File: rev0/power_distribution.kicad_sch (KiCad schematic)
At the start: 81 parts, among them Q1 PMOS, Q10 2PNP, Q11 2NPN, Q12 PMOS, Q13 2PNP, Q14 2PNP, Q15 2PNP, Q2 PMOS, Q3 2NPN, Q4 PMOS, Q5 PMOS, Q6 PMOS, Q7 PMOS, Q8 2NPN, Q9 PMOS, U1 PAC1954

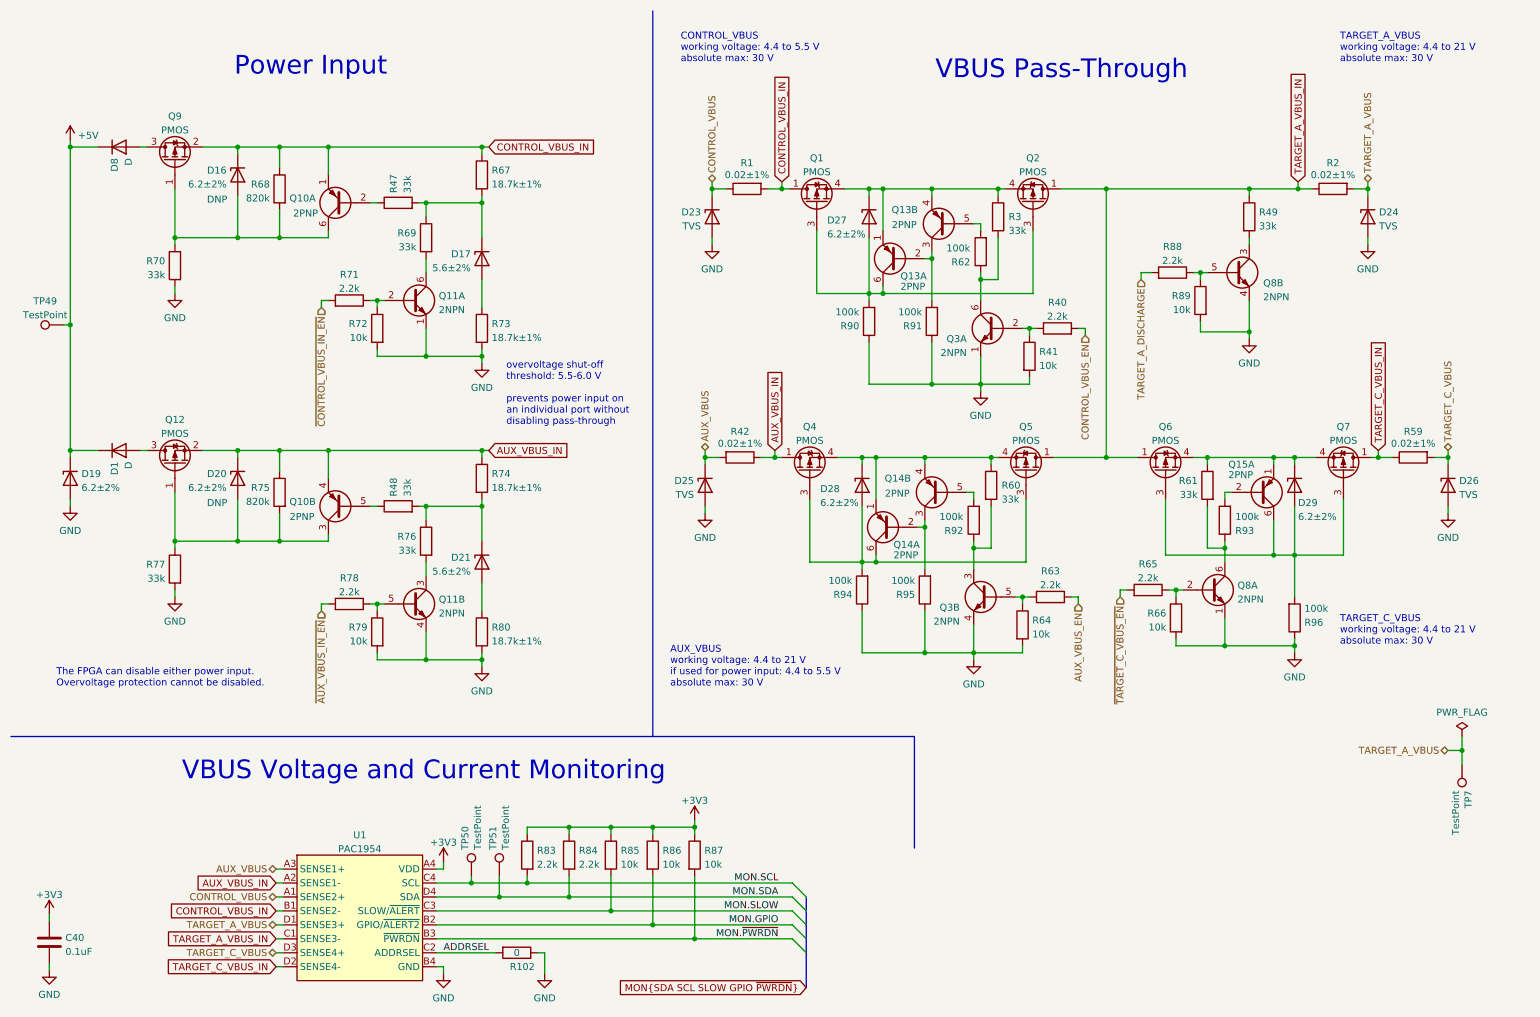
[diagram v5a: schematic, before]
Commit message: hardware: update pull-up and pull-down resistors
- do not populate unnecessary resistors
- remove some unnecessary 0 ohm resistors
- add recommended FPGA resistors
- add recommended MCU resistors
- update hardware version detection pin strap
- change CONTROL port USB switch default to MCU
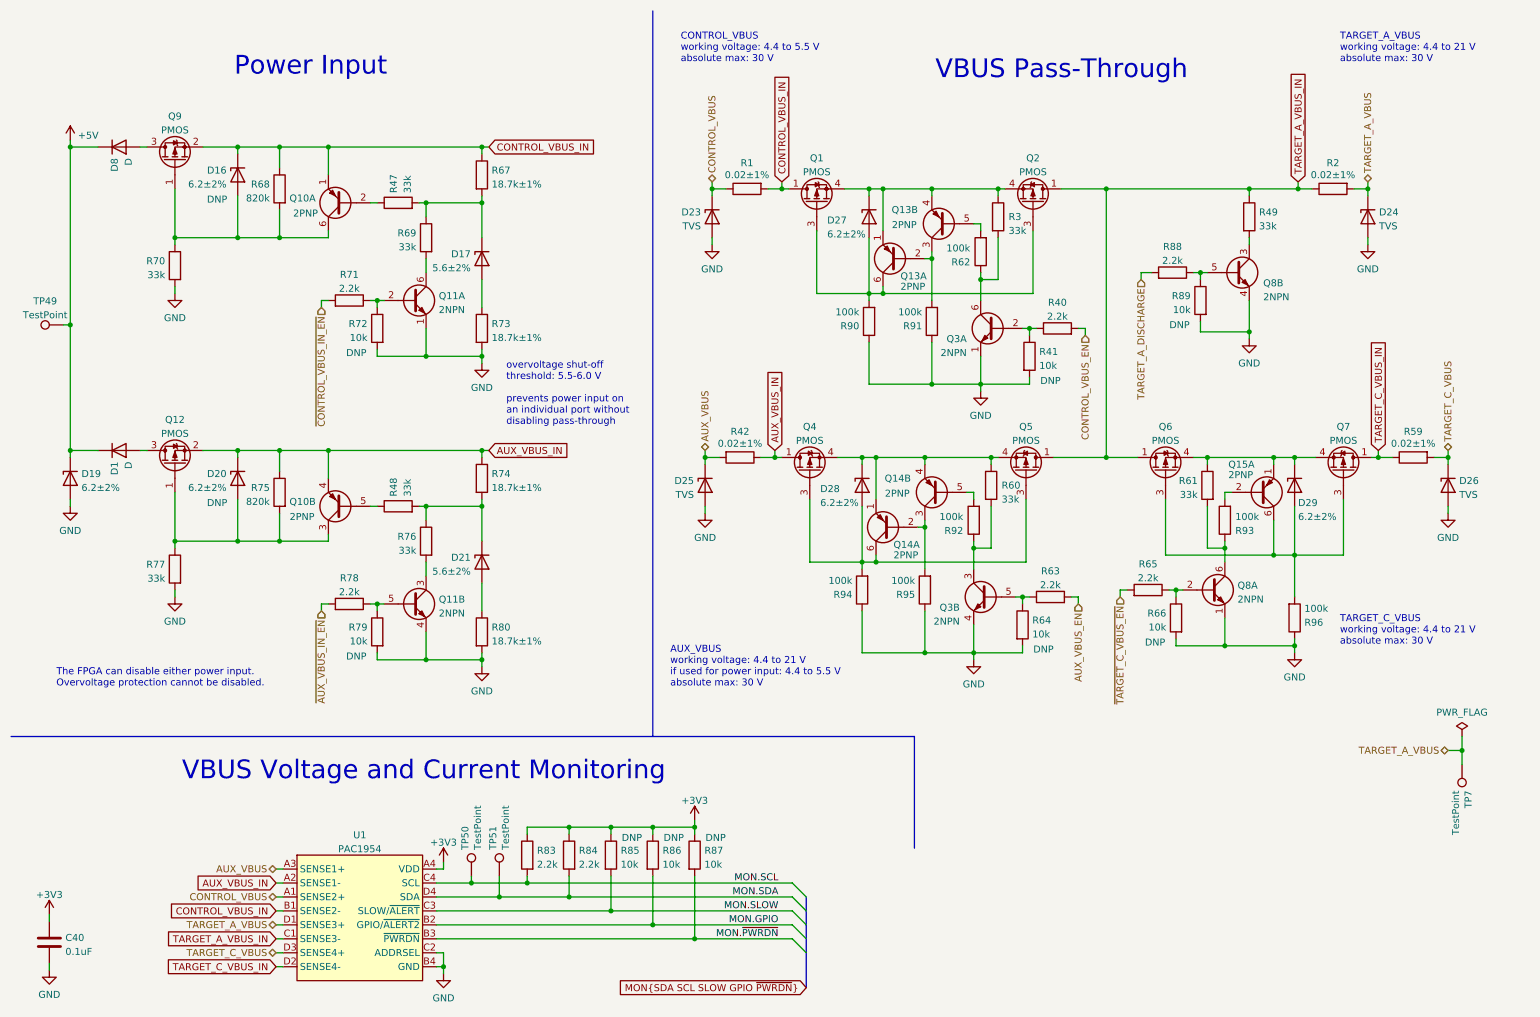
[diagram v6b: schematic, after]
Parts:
- removed R102: 0, Resistor_SMD:R_0402_1005Metric, symbol Device:R
- R41, R64, R66, R72, R79, R85, R86, R87, R89: DNP (none) -> DNP
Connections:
- net ADDRSEL is gone; now on net GND: U1.C2 (ADDRSEL)
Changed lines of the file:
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@@
   (junction (at 23.495 69.85) (diameter 0) (color 0 0 0 0)
   )
+  (junction (at 91.44 186.69) (diameter 0) (color 0 0 0 0)
+  )
   (junction (at 79.375 120.65) (diameter 0) (color 0 0 0 0)
   )
@@
     (stroke (width 0) (type default) (color 0 0 0 0))
   )
+  (wire (pts (xy 91.44 184.15) (xy 91.44 186.69))
+    (stroke (width 0) (type default) (color 0 0 0 0))
+  )
   (wire (pts (xy 78.105 102.87) (xy 79.375 102.87))
     (stroke (width 0) (type default) (color 0 0 0 0))
@@
     (stroke (width 0) (type default) (color 0 0 0 0))
   )
-  (wire (pts (xy 108.585 184.15) (xy 109.855 184.15))
-    (stroke (width 0) (type default) (color 0 0 0 0))
-  )
   (wire (pts (xy 90.17 186.69) (xy 91.44 186.69))
     (stroke (width 0) (type default) (color 0 0 0 0))
@@
     (stroke (width 0) (type default) (color 0 0 0 0))
   )
-  (wire (pts (xy 90.17 184.15) (xy 100.965 184.15))
+  (wire (pts (xy 90.17 184.15) (xy 91.44 184.15))
     (stroke (width 0) (type default) (color 0 0 0 0))
   )
@@
     (stroke (width 0) (type default) (color 0 0 0 0))
   )
-  (wire (pts (xy 109.855 184.15) (xy 109.855 187.96))
-    (stroke (width 0) (type default) (color 0 0 0 0))
-  )
   (wire (pts (xy 79.375 74.295) (xy 79.375 75.565))
     (stroke (width 0) (type default) (color 0 0 0 0))
@@
     (effects (font (size 1.27 1.27)) (justify right bottom))
   )
-  (label "ADDRSEL" (at 91.44 184.15 0)
-    (effects (font (size 1.27 1.27)) (justify left bottom))
-  )
   (label "MON.~{PWRDN}" (at 152.4 181.61 180)
     (effects (font (size 1.27 1.27)) (justify right bottom))
@@
       (effects (font (size 1.27 1.27)) hide)
     )
+    (property "DNP" "DNP" (id 8) (at 75.565 74.93 0))
     (pin "1")
     (pin "2")
@@
       (effects (font (size 1.27 1.27)) hide)
     )
+    (property "DNP" "DNP" (id 8) (at 220.98 127.635 0))
     (pin "1")
     (pin "2")
@@
       (effects (font (size 1.27 1.27)) hide)
     )
+    (property "DNP" "DNP" (id 8) (at 225.425 69.85 0))
     (pin "1")
     (pin "2")
@@
       (effects (font (size 1.27 1.27)) hide)
     )
+    (property "DNP" "DNP" (id 8) (at 75.565 130.175 0))
     (pin "1")
     (pin "2")
@@
       (effects (font (size 1.27 1.27)) hide)
     )
+    (property "DNP" "DNP" (id 8) (at 140.97 163.195 0))
     (pin "1")
     (pin "2")
@@
     (pin "2")
   )
-  (symbol (lib_id "power:GND") (at 109.855 187.96 0) (mirror y) (unit 1)
-    (in_bom yes) (on_board yes) (fields_autoplaced)
-    (property "Reference" "#PWR065" (id 0) (at 109.855 194.31 0)
-      (effects (font (size 1.27 1.27)) hide)
-    )
-    (property "Value" "GND" (id 1) (at 109.855 192.4034 0))
-    (property "Footprint" "" (id 2) (at 109.855 187.96 0)
-      (effects (font (size 1.27 1.27)) hide)
-    )
-    (property "Datasheet" "" (id 3) (at 109.855 187.96 0)
-      (effects (font (size 1.27 1.27)) hide)
-    )
-    (pin "1")
-  )
   (symbol (lib_id "power:GND") (at 238.125 72.39 0) (unit 1)
     (in_bom yes) (on_board yes) (fields_autoplaced)
@@
       (effects (font (size 1.27 1.27)) hide)
     )
+    (property "DNP" "DNP" (id 8) (at 125.73 163.195 0))
     (pin "1")
     (pin "2")
@@
       (effects (font (size 1.27 1.27)) hide)
     )
+    (property "DNP" "DNP" (id 8) (at 201.93 80.01 0))
     (pin "1")
     (pin "2")
@@
       (effects (font (size 1.27 1.27)) hide)
     )
+    (property "DNP" "DNP" (id 8) (at 133.35 163.195 0))
     (pin "1")
     (pin "2")
@@
       (effects (font (size 1.27 1.27)) hide)
     )
+    (property "DNP" "DNP" (id 8) (at 200.66 128.905 0))
     (pin "1")
     (pin "2")
@@
       (effects (font (size 1.27 1.27)) hide)
     )
-    (pin "1")
-    (pin "2")
-  )
-  (symbol (lib_id "Device:R") (at 104.775 184.15 270) (unit 1)
-    (in_bom yes) (on_board yes)
-    (property "Reference" "R102" (id 0) (at 103.505 186.69 90)
-      (effects (font (size 1.27 1.27)) (justify left))
-    )
-    (property "Value" "0" (id 1) (at 104.775 184.15 90))
-    (property "Footprint" "Resistor_SMD:R_0402_1005Metric" (id 2) (at 104.775 182.372 90)
-      (effects (font (size 1.27 1.27)) hide)
-    )
-    (property "Datasheet" "~" (id 3) (at 104.775 184.15 0)
-      (effects (font (size 1.27 1.27)) hide)
-    )
-    (property "Part Number" "RC0402FR-070RL" (id 4) (at 104.775 184.15 0)
-      (effects (font (size 1.27 1.27)) hide)
-    )
-    (property "Substitution" "any equivalent" (id 5) (at 104.775 184.15 0)
-      (effects (font (size 1.27 1.27)) hide)
-    )
-    (property "Description" "RES 0 OHM JUMPER 1/16W 0402" (id 6) (at 104.775 184.15 0)
-      (effects (font (size 1.27 1.27)) hide)
-    )
-    (property "Manufacturer" "Yageo" (id 7) (at 104.775 184.15 0)
-      (effects (font (size 1.27 1.27)) hide)
-    )

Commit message: hardware: update FET component selection
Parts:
- Q1, Q2, Q4, Q5, Q6, Q7: Manufacturer Diodes Inc. -> Vishay Siliconix; Part Number DMP3028LFDE-7 -> SIA483ADJ-T1-GE3; Substitution DMP3028LFDE-13, Nexperia PMPB27EP,115, PMPB16EPX, Vishay SI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 -> SIA483DJ-T1-GE3, Nexperia PMPB16EPX, PMPB27EP,115
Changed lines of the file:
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@@
       (effects (font (size 1.27 1.27)) hide)
     )
-    (property "Datasheet" "https://www.diodes.com/assets/Datasheets/DMP3028LFDE.pdf" (id 3) (at 255.27 96.52 0)
-      (effects (font (size 1.27 1.27)) hide)
-    )
-    (property "Manufacturer" "Diodes Inc." (id 4) (at 255.27 96.52 0)
-      (effects (font (size 1.27 1.27)) hide)
-    )
-    (property "Part Number" "DMP3028LFDE-7" (id 5) (at 255.27 96.52 0)
-      (effects (font (size 1.27 1.27)) hide)
-    )
-    (property "Description" "MOSFET P-CH 30V 6.8A 6UDFN" (id 6) (at 255.27 96.52 0)
-      (effects (font (size 1.27 1.27)) hide)
-    )
-    (property "Substitution" "DMP3028LFDE-13, Nexperia PMPB27EP,115, PMPB16EPX, Vishay SIA469DJ-T1-GE3,  SIA483ADJ-T1-GE3, SIA483DJ-T1-GE3, Toshiba SSM6J507NU,LF" (id 7) (at 255.27 96.52 0)
+    (property "Datasheet" "https://www.vishay.com/docs/77080/sia483adj.pdf" (id 3) (at 255.27 96.52 0)
+      (effects (font (size 1.27 1.27)) hide)
+    )
+    (property "Manufacturer" "Vishay Siliconix" (id 4) (at 255.27 96.52 0)
+      (effects (font (size 1.27 1.27)) hide)
+    )
+    (property "Part Number" "SIA483ADJ-T1-GE3" (id 5) (at 255.27 96.52 0)
+      (effects (font (size 1.27 1.27)) hide)
+    )
+    (property "Description" "MOSFET P-CH 30V 10.6A/12A PPAK" (id 6) (at 255.27 96.52 0)
+      (effects (font (size 1.27 1.27)) hide)
+    )
+    (property "Substitution" "SIA483DJ-T1-GE3, Nexperia PMPB16EPX, PMPB27EP,115" (id 7) (at 255.27 96.52 0)
       (effects (font (size 1.27 1.27)) hide)
     )
@@
       (effects (font (size 1.27 1.27)) hide)
     )
-    (property "Datasheet" "https://www.diodes.com/assets/Datasheets/DMP3028LFDE.pdf" (id 3) (at 197.485 96.52 0)
-      (effects (font (size 1.27 1.27)) hide)
-    )
-    (property "Manufacturer" "Diodes Inc." (id 4) (at 197.485 96.52 0)
-      (effects (font (size 1.27 1.27)) hide)
-    )
-    (property "Part Number" "DMP3028LFDE-7" (id 5) (at 197.485 96.52 0)
-      (effects (font (size 1.27 1.27)) hide)
-    )
-    (property "Description" "MOSFET P-CH 30V 6.8A 6UDFN" (id 6) (at 197.485 96.52 0)
-      (effects (font (size 1.27 1.27)) hide)
-    )
-    (property "Substitution" "DMP3028LFDE-13, Nexperia PMPB27EP,115, PMPB16EPX, Vishay SIA469DJ-T1-GE3,  SIA483ADJ-T1-GE3, SIA483DJ-T1-GE3, Toshiba SSM6J507NU,LF" (id 7) (at 197.485 96.52 0)
+    (property "Datasheet" "https://www.vishay.com/docs/77080/sia483adj.pdf" (id 3) (at 197.485 96.52 0)
+      (effects (font (size 1.27 1.27)) hide)
+    )
+    (property "Manufacturer" "Vishay Siliconix" (id 4) (at 197.485 96.52 0)
+      (effects (font (size 1.27 1.27)) hide)
+    )
+    (property "Part Number" "SIA483ADJ-T1-GE3" (id 5) (at 197.485 96.52 0)
+      (effects (font (size 1.27 1.27)) hide)
+    )
+    (property "Description" "MOSFET P-CH 30V 10.6A/12A PPAK" (id 6) (at 197.485 96.52 0)
+      (effects (font (size 1.27 1.27)) hide)
+    )
+    (property "Substitution" "SIA483DJ-T1-GE3, Nexperia PMPB16EPX, PMPB27EP,115" (id 7) (at 197.485 96.52 0)
       (effects (font (size 1.27 1.27)) hide)
     )
@@
       (effects (font (size 1.27 1.27)) hide)
     )
-    (property "Datasheet" "https://www.diodes.com/assets/Datasheets/DMP3028LFDE.pdf" (id 3) (at 159.385 47.625 0)
-      (effects (font (size 1.27 1.27)) hide)
-    )
-    (property "Manufacturer" "Diodes Inc." (id 4) (at 159.385 47.625 0)
-      (effects (font (size 1.27 1.27)) hide)
-    )
-    (property "Part Number" "DMP3028LFDE-7" (id 5) (at 159.385 47.625 0)
-      (effects (font (size 1.27 1.27)) hide)
-    )
-    (property "Description" "MOSFET P-CH 30V 6.8A 6UDFN" (id 6) (at 159.385 47.625 0)
-      (effects (font (size 1.27 1.27)) hide)
-    )
-    (property "Substitution" "DMP3028LFDE-13, Nexperia PMPB27EP,115, PMPB16EPX, Vishay SIA469DJ-T1-GE3,  SIA483ADJ-T1-GE3, SIA483DJ-T1-GE3, Toshiba SSM6J507NU,LF" (id 7) (at 159.385 47.625 0)
+    (property "Datasheet" "https://www.vishay.com/docs/77080/sia483adj.pdf" (id 3) (at 159.385 47.625 0)
+      (effects (font (size 1.27 1.27)) hide)
+    )
+    (property "Manufacturer" "Vishay Siliconix" (id 4) (at 159.385 47.625 0)
+      (effects (font (size 1.27 1.27)) hide)
+    )
+    (property "Part Number" "SIA483ADJ-T1-GE3" (id 5) (at 159.385 47.625 0)
+      (effects (font (size 1.27 1.27)) hide)
+    )
+    (property "Description" "MOSFET P-CH 30V 10.6A/12A PPAK" (id 6) (at 159.385 47.625 0)
+      (effects (font (size 1.27 1.27)) hide)
+    )
+    (property "Substitution" "SIA483DJ-T1-GE3, Nexperia PMPB16EPX, PMPB27EP,115" (id 7) (at 159.385 47.625 0)
       (effects (font (size 1.27 1.27)) hide)
     )
@@
       (effects (font (size 1.27 1.27)) hide)
     )
-    (property "Datasheet" "https://www.diodes.com/assets/Datasheets/DMP3028LFDE.pdf" (id 3) (at 158.115 96.52 0)
-      (effects (font (size 1.27 1.27)) hide)
-    )
-    (property "Manufacturer" "Diodes Inc." (id 4) (at 158.115 96.52 0)
-      (effects (font (size 1.27 1.27)) hide)
-    )
-    (property "Part Number" "DMP3028LFDE-7" (id 5) (at 158.115 96.52 0)
-      (effects (font (size 1.27 1.27)) hide)
-    )
-    (property "Description" "MOSFET P-CH 30V 6.8A 6UDFN" (id 6) (at 158.115 96.52 0)
-      (effects (font (size 1.27 1.27)) hide)
-    )
-    (property "Substitution" "DMP3028LFDE-13, Nexperia PMPB27EP,115, PMPB16EPX, Vishay SIA469DJ-T1-GE3,  SIA483ADJ-T1-GE3, SIA483DJ-T1-GE3, Toshiba SSM6J507NU,LF" (id 7) (at 158.115 96.52 0)
+    (property "Datasheet" "https://www.vishay.com/docs/77080/sia483adj.pdf" (id 3) (at 158.115 96.52 0)
+      (effects (font (size 1.27 1.27)) hide)
+    )
+    (property "Manufacturer" "Vishay Siliconix" (id 4) (at 158.115 96.52 0)
+      (effects (font (size 1.27 1.27)) hide)
+    )
+    (property "Part Number" "SIA483ADJ-T1-GE3" (id 5) (at 158.115 96.52 0)
+      (effects (font (size 1.27 1.27)) hide)
+    )
+    (property "Description" "MOSFET P-CH 30V 10.6A/12A PPAK" (id 6) (at 158.115 96.52 0)
+      (effects (font (size 1.27 1.27)) hide)
+    )
+    (property "Substitution" "SIA483DJ-T1-GE3, Nexperia PMPB16EPX, PMPB27EP,115" (id 7) (at 158.115 96.52 0)
       (effects (font (size 1.27 1.27)) hide)
     )
@@
       (effects (font (size 1.27 1.27)) hide)
     )
-    (property "Datasheet" "https://www.diodes.com/assets/Datasheets/DMP3028LFDE.pdf" (id 3) (at 222.885 96.52 0)
-      (effects (font (size 1.27 1.27)) hide)
-    )
-    (property "Manufacturer" "Diodes Inc." (id 4) (at 222.885 96.52 0)
-      (effects (font (size 1.27 1.27)) hide)
-    )
-    (property "Part Number" "DMP3028LFDE-7" (id 5) (at 222.885 96.52 0)
-      (effects (font (size 1.27 1.27)) hide)
-    )
-    (property "Description" "MOSFET P-CH 30V 6.8A 6UDFN" (id 6) (at 222.885 96.52 0)
-      (effects (font (size 1.27 1.27)) hide)
-    )
-    (property "Substitution" "DMP3028LFDE-13, Nexperia PMPB27EP,115, PMPB16EPX, Vishay SIA469DJ-T1-GE3,  SIA483ADJ-T1-GE3, SIA483DJ-T1-GE3, Toshiba SSM6J507NU,LF" (id 7) (at 222.885 96.52 0)
+    (property "Datasheet" "https://www.vishay.com/docs/77080/sia483adj.pdf" (id 3) (at 222.885 96.52 0)
+      (effects (font (size 1.27 1.27)) hide)
+    )
+    (property "Manufacturer" "Vishay Siliconix" (id 4) (at 222.885 96.52 0)
+      (effects (font (size 1.27 1.27)) hide)
+    )
+    (property "Part Number" "SIA483ADJ-T1-GE3" (id 5) (at 222.885 96.52 0)
+      (effects (font (size 1.27 1.27)) hide)
+    )
+    (property "Description" "MOSFET P-CH 30V 10.6A/12A PPAK" (id 6) (at 222.885 96.52 0)
+      (effects (font (size 1.27 1.27)) hide)
+    )
+    (property "Substitution" "SIA483DJ-T1-GE3, Nexperia PMPB16EPX, PMPB27EP,115" (id 7) (at 222.885 96.52 0)
       (effects (font (size 1.27 1.27)) hide)
     )
@@
       (effects (font (size 1.27 1.27)) hide)
     )
-    (property "Datasheet" "https://www.diodes.com/assets/Datasheets/DMP3028LFDE.pdf" (id 3) (at 198.755 47.625 0)
-      (effects (font (size 1.27 1.27)) hide)
-    )
-    (property "Manufacturer" "Diodes Inc." (id 4) (at 198.755 47.625 0)
-      (effects (font (size 1.27 1.27)) hide)
-    )
-    (property "Part Number" "DMP3028LFDE-7" (id 5) (at 198.755 47.625 0)
-      (effects (font (size 1.27 1.27)) hide)
-    )
-    (property "Description" "MOSFET P-CH 30V 6.8A 6UDFN" (id 6) (at 198.755 47.625 0)
-      (effects (font (size 1.27 1.27)) hide)
-    )
-    (property "Substitution" "DMP3028LFDE-13, Nexperia PMPB27EP,115, PMPB16EPX, Vishay SIA469DJ-T1-GE3,  SIA483ADJ-T1-GE3, SIA483DJ-T1-GE3, Toshiba SSM6J507NU,LF" (id 7) (at 198.755 47.625 0)
-      (effects (font (size 1.27 1.27)) hide)
-    )
+    (property "Datasheet" "https://www.vishay.com/docs/77080/sia483adj.pdf" (id 3) (at 198.755 47.625 0)
+      (effects (font (size 1.27 1.27)) hide)
+    )
+    (property "Manufacturer" "Vishay Siliconix" (id 4) (at 198.755 47.625 0)
+      (effects (font (size 1.27 1.27)) hide)
+    )
+    (property "Part Number" "SIA483ADJ-T1-GE3" (id 5) (at 198.755 47.625 0)
+      (effects (font (size 1.27 1.27)) hide)
+    )
+    (property "Description" "MOSFET P-CH 30V 10.6A/12A PPAK" (id 6) (at 198.755 47.625 0)
+      (effects (font (size 1.27 1.27)) hide)
+    )
+    (property "Substitution" "SIA483DJ-T1-GE3, Nexperia PMPB16EPX, PMPB27EP,115" (id 7) (at 198.755 47.625 0)
+      (effects (font (size 1.27 1.27)) hide)
+    )
